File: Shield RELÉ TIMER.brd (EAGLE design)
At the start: 130 x 90 mm, 54 parts, among them K1 JS-M1-9V-5, K2 JS-M1-9V-5, K3 JS-M1-9V-5, K4 JS-M1-9V-5, K5 JS-M1-9V-5, K6 JS-M1-9V-5, M1 ARDUINO-NANO-3.0, Q1 BC548, Q2 BC548, Q3 BC548, Q4 BC548, Q5 BC548, Q6 BC548

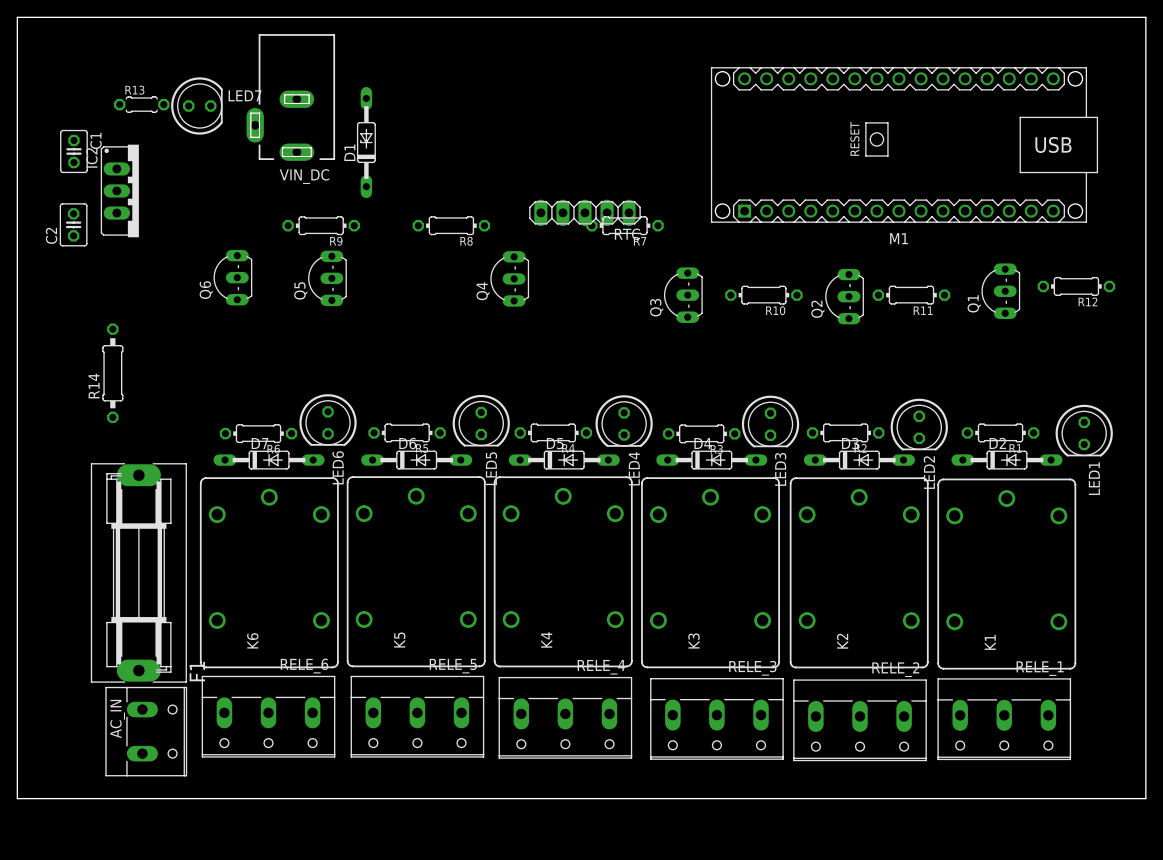
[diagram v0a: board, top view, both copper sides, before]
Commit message: Modulo
Separação modulo com reles
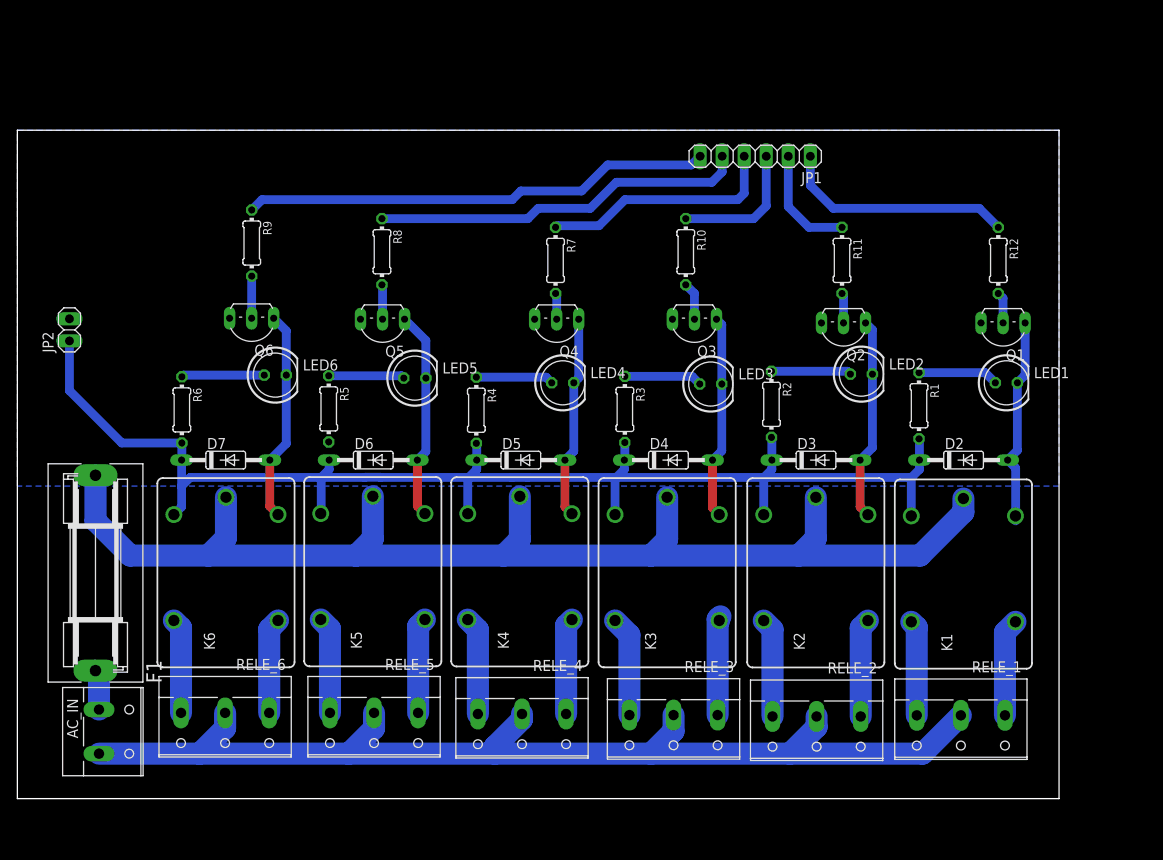
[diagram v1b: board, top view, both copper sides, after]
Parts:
- removed C1, C2: (no value), rcl:C025-030X050
- removed D1: 1N821, diode:DO35Z10
- removed IC2: (no value), v-reg:78XXS
- removed LED7: (no value), led:LED5MM
- removed M1: ARDUINO-NANO-3.0, diy-modules:ARDUINO-NANO-3.0
- removed R13: (no value), rcl:0204/5
- removed R14: (no value), eagle-ltspice:0207/10
- removed RTC: (no value), pinhead:1X05
- removed VIN_DC: DCJ0202 9V, con-jack:DCJ0202
- added JP1: (no value), pinhead:1X06
- added JP2: (no value), pinhead:1X02
- moved LED1 10.7 mm to (113.9, 47.9), turned to 0 degrees
- moved R10 10.3 mm to (77.0, 63.0), turned to 270 degrees
- moved R1 9.90 mm to (103.9, 45.3), turned to 270 degrees
- moved R12 9.49 mm to (113.0, 62.0), turned to 270 degrees
- moved R5 9.45 mm to (35.9, 44.9), turned to 270 degrees
- moved R3 9.29 mm to (70.0, 44.8), turned to 270 degrees
- moved Q5 9.28 mm to (42.1, 54.0), turned to 180 degrees
- moved LED5 9.27 mm to (45.8, 48.4), turned to 0 degrees
- moved R4 9.25 mm to (52.9, 44.7), turned to 270 degrees
- moved R6 9.24 mm to (18.9, 44.8), turned to 270 degrees
- moved R2 9.16 mm to (86.9, 45.4), turned to 270 degrees
- moved LED2 9.06 mm to (97.2, 48.9), turned to 0 degrees
- moved R11 8.94 mm to (95.0, 62.0), turned to 270 degrees
- moved R7 8.94 mm to (62.0, 62.0), turned to 270 degrees
- moved Q4 8.55 mm to (62.1, 54.0), turned to 180 degrees
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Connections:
- removed net 3V3: M1.J2.14
- removed net A0: M1.J2.12
- removed net A1: M1.J2.11
- removed net A2: M1.J2.10
- removed net A3: M1.J2.9
- removed net A6: M1.J2.6, RTC.1
- removed net D10: M1.J1.13
- removed net D6: M1.J1.9
- removed net D7: M1.J1.10
- removed net D8: M1.J1.11
- removed net D9: M1.J1.12
- removed net GND.1: M1.J1.4
- removed net N$19: LED7.A, R13.2
- removed net N$20: IC2.OUT, R14.1
- removed net SCL: M1.J2.7, RTC.2
- removed net SDA: M1.J2.8, RTC.3
- removed net VIN: C1.1, D1.C, IC2.IN, M1.J2.1
- removed net VIN5: M1.J2.4, RTC.4
- net +5V: now also JP2.1; no longer C2.1, R13.1, R14.2
- net D11: now also JP1.2; no longer M1.J1.14
- net D12: now also JP1.1; no longer M1.J1.15
- net D2: now also JP1.6; no longer M1.J1.5
- net D3: now also JP1.5; no longer M1.J1.6
- net D4: now also JP1.4; no longer M1.J1.7
- net D5: now also JP1.3; no longer M1.J1.8
- net GND: now also JP2.2; no longer C1.2, C2.2, IC2.GND, LED7.K, M1.J2.2, RTC.5, VIN_DC.2, VIN_DC.3
- net N$17: now also Q1.B, R12.2; no longer D1.A, VIN_DC.1
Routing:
- net +5V: track 0.00 -> 156.8 mm
- net PHASE: track 0.00 -> 148.4 mm
- net RETURN: track 0.00 -> 129.9 mm
- net D2: track 0.00 -> 54.2 mm
- net D3: track 0.00 -> 43.2 mm
- net D4: track 0.00 -> 27.6 mm
- net D12: track 0.00 -> 27.0 mm
- net N$13: track 0.00 -> 24.4 mm
- net N$10: track 0.00 -> 24.2 mm
- net N$35: track 0.00 -> 24.0 mm
- net N$4: track 0.00 -> 23.5 mm
- net N$7: track 0.00 -> 23.4 mm
- net N$1: track 0.00 -> 23.4 mm
- net D5: track 0.00 -> 15.6 mm
- net D11: track 0.00 -> 13.0 mm
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- added copper zone on layer 16, net GND
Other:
- board size 130 x 90 mm -> 120 x 77 mm

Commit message: Relay module
Develop three relay module
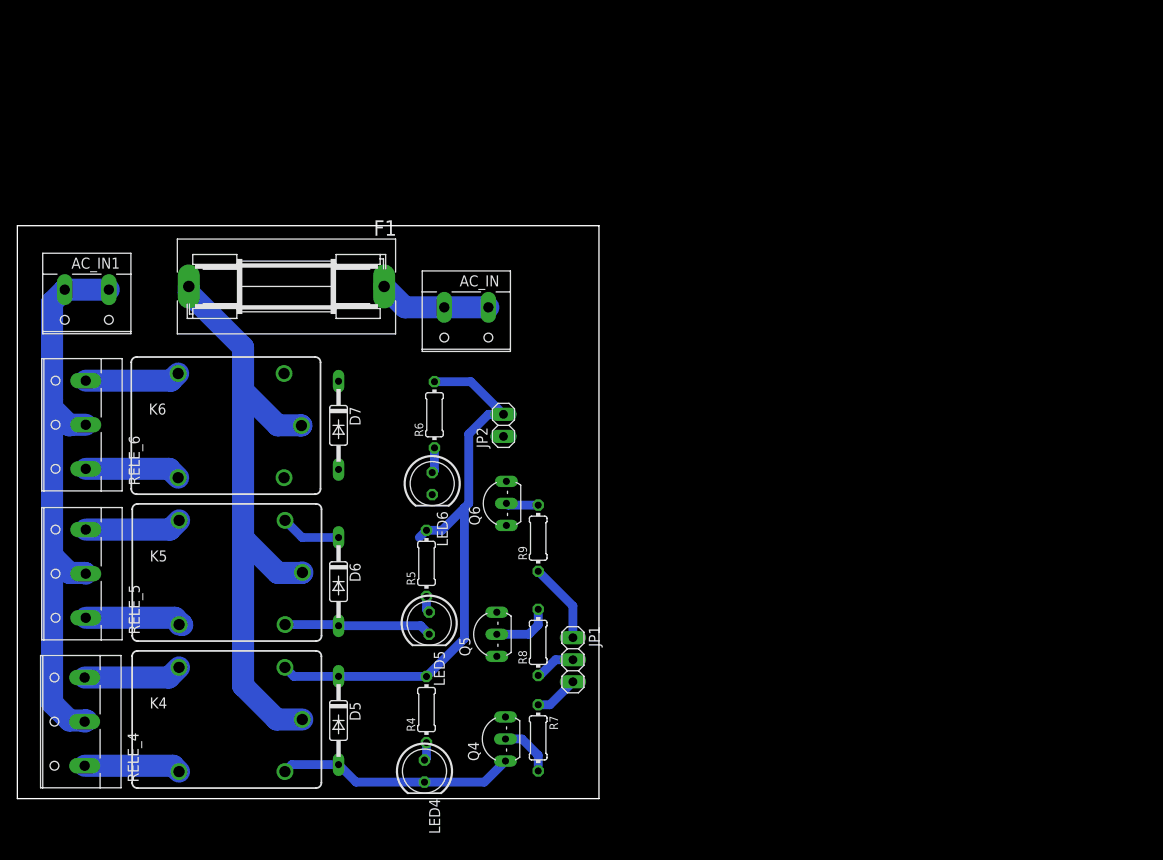
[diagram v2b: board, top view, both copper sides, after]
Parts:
- removed D2, D3, D4: 1N4148DO35-10, diode:DO35-10
- removed K1, K2, K3: JS-M1-9V-5, relay:JS-M
- removed LED1, LED2, LED3: (no value), led:LED5MM
- removed Q1, Q2, Q3: BC548, transistor-npn:TO92-EBC
- removed R1, R10, R11, R12, R2, R3: (no value), eagle-ltspice:0204/7
- removed RELE_1, RELE_2, RELE_3: (no value), con-wago-508:W237-133
- added AC_IN1: 220V, con-wago-508:W237-132
- JP1: device pinhead:1X06 -> pinhead:1X03
- moved AC_IN 63.8 mm to (51.7, 56.0), turned to 180 degrees
- moved JP1 61.7 mm to (64.0, 16.0), turned to 270 degrees
- moved R7 55.0 mm to (60.0, 7.00)
- moved JP2 51.2 mm to (56.0, 43.0)
- moved RELE_4 51.0 mm to (7.12, 8.87), turned to 90 degrees
- moved R8 48.5 mm to (60.0, 18.0), turned to 90 degrees
- moved Q4 47.6 mm to (55.0, 6.87), turned to 90 degrees
- moved LED4 47.5 mm to (46.9, 3.17), turned to 270 degrees
- moved R9 47.4 mm to (60.0, 30.0), turned to 90 degrees
- moved F1 39.7 mm to (31.0, 59.0), turned to 180 degrees
- moved K4 37.8 mm to (24.1, 9.12), turned to 0 degrees
- moved RELE_5 37.7 mm to (7.24, 25.9), turned to 90 degrees
- moved RELE_6 37.7 mm to (7.24, 43.1), turned to 90 degrees
- moved Q5 37.0 mm to (54.0, 18.9), turned to 90 degrees
- moved D5 36.6 mm to (37.0, 9.00), turned to 270 degrees
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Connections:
- removed net D11: JP1.2, R11.1
- removed net D12: JP1.1, R12.1
- removed net D5: JP1.3, R10.1
- removed net N$1: D3.A, K2.2, LED2.K, Q2.C
- removed net N$15: Q3.B, R10.2
- removed net N$17: Q1.B, R12.2
- removed net N$18: Q2.B, R11.2
- removed net N$35: D2.A, K1.2, LED1.K, Q1.C
- removed net N$4: D4.A, K3.2, LED3.K, Q3.C
- removed net N$6: LED1.A, R1.1
- removed net N$8: LED2.A, R2.1
- removed net N$9: LED3.A, R3.1
- removed net NC_1: K1.NC, RELE_1.1
- removed net NC_2: K2.NC, RELE_2.1
- removed net NC_3: K3.NC, RELE_3.1
- removed net NO_1: K1.NO, RELE_1.3
- removed net NO_2: K2.NO, RELE_2.3
- removed net NO_3: K3.NO, RELE_3.3
- net +5V: now also JP2.2; no longer D2.C, D3.C, D4.C, JP2.1, K1.1, K2.1, K3.1, R1.2, R2.2, R3.2
- net D2: now also JP1.1; no longer JP1.6
- net D3: now also JP1.2; no longer JP1.5
- net D4: now also JP1.3; no longer JP1.4
- net GND: now also JP2.1; no longer JP2.2, Q1.E, Q2.E, Q3.E
- net N$16: now also AC_IN.2
- net PHASE: no longer K1.C, K2.C, K3.C
- net RETURN: now also AC_IN1.1, AC_IN1.2; no longer AC_IN.2, RELE_1.2, RELE_2.2, RELE_3.2
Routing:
- net +5V: track 156.8 -> 74.7 mm
- net PHASE: track 148.4 -> 73.9 mm
- net RETURN: track 129.9 -> 67.8 mm
- net D2: track 54.2 -> 9.31 mm
- net D3: track 43.2 -> 4.75 mm
- net D12: track 27.0 -> 0.00 mm
- net N$13: track 24.4 -> 0.07 mm
- net N$35: track 24.0 -> 0.00 mm
- net N$4: track 23.5 -> 0.00 mm
- net N$1: track 23.4 -> 0.00 mm
- net D4: track 27.6 -> 5.10 mm
- net D5: track 15.6 -> 0.00 mm
- net D11: track 13.0 -> 0.00 mm
- net NC_3: track 11.8 -> 0.00 mm
- net NO_3: track 11.6 -> 0.00 mm
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- removed copper zone on layer 16, net GND
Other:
- board size 120 x 77 mm -> 67 x 66 mm
